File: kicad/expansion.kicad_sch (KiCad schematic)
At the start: 8 parts, among them J10 Slot 2, J11 Slot 3, J12 Slot 4, J9 Slot 1

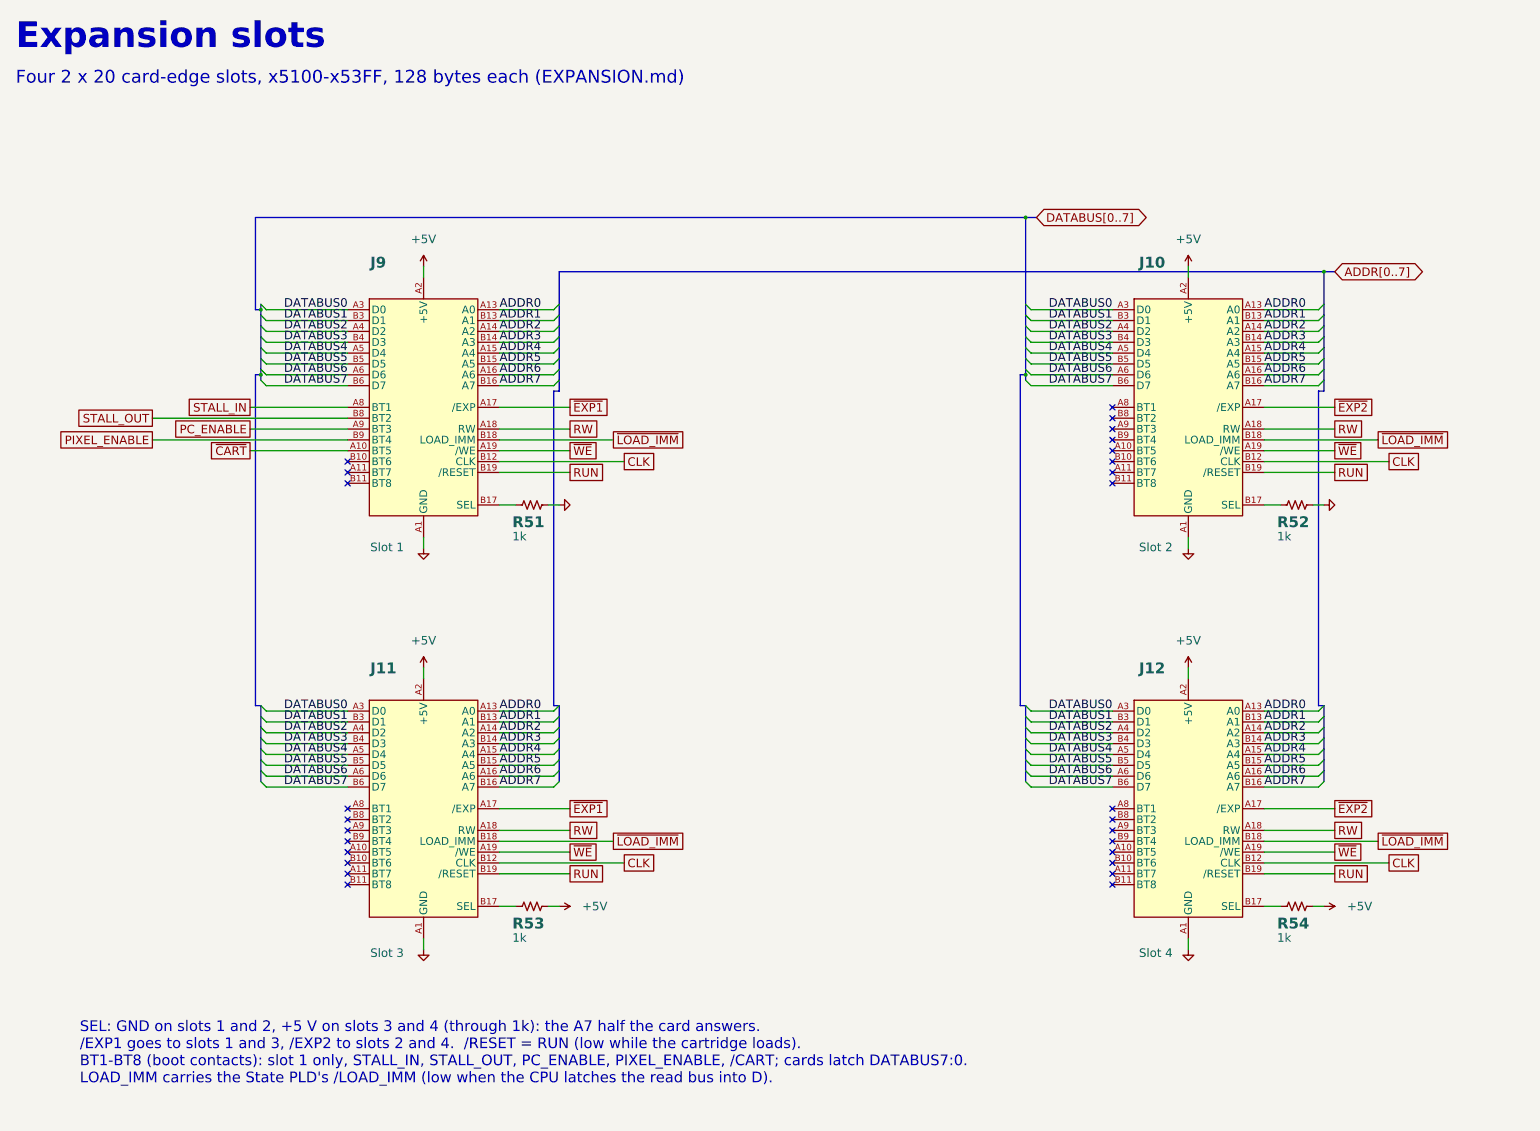
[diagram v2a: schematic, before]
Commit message: Expansion slots 2 x 25 (Sullins EBC25DRXH): A15:A8 and PIXEL_ENABLE on every slot
Contacts 1-20 unchanged; 21-24 = A8-A15, A25 = PIXEL_ENABLE, B25 = GND, so a
card can follow the video reads (HDMI capture) or CPU writes.  Footprint, 3D
model and shell keepout from Sullins drawing C10881 rev P (card 86.7 mm,
keepout 93.7 x 25.04 mm, 3.18 mm ear holes 78.11 apart, M3 x 12 + nut).
Schematic, netlist check, BOM (Digi-Key S3322-ND $6.63), EXPANSION.md
("Video capture cards"), CASE.md, BRINGUP.md, shell keepout drawing.
Main board file untouched: Justin updates the PCB from the schematic.

Co-Authored-By: Claude Opus 5.5 <noreply@anthropic.com>
Claude-Session: https://claude.ai/code/session_01DnW5SUDtmC2C2nXUS4xVk2
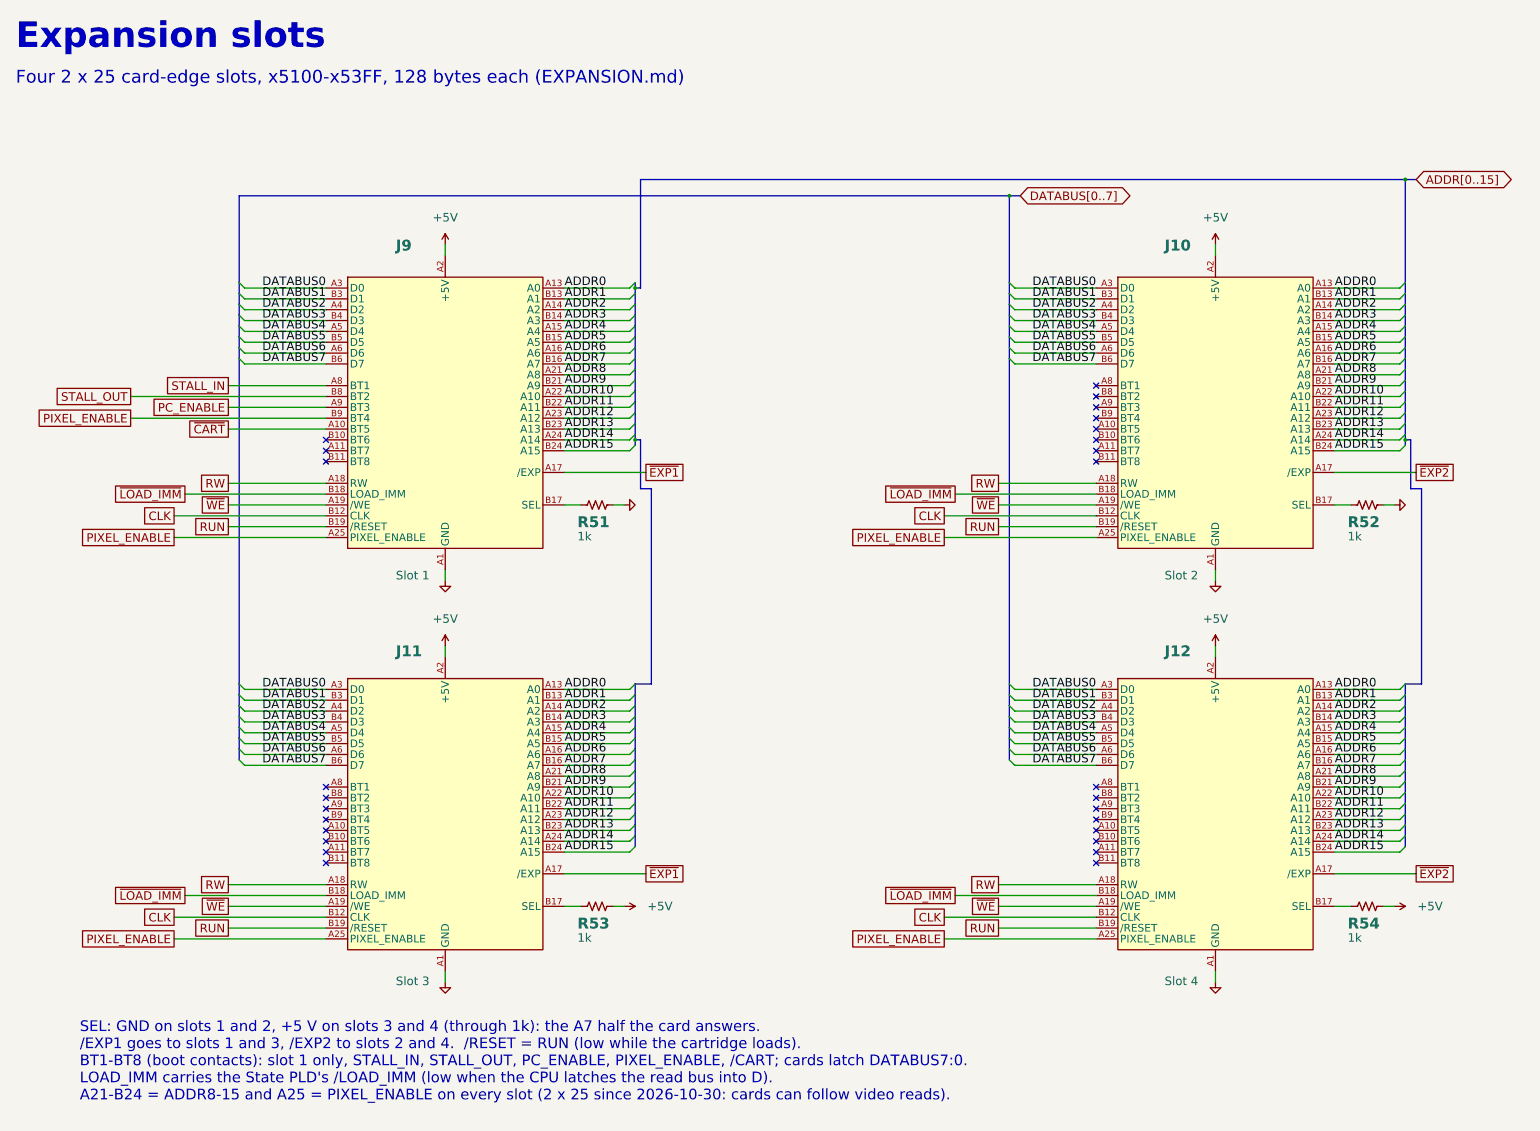
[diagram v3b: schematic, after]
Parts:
- J10, J11, J12, J9: footprint placard:CardEdge_2x20_P2.54mm_Vertical -> placard:CardEdge_2x25_P2.54mm_Vertical; MPN EBC20DCAN -> EBC25DRXH
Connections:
- net GND: now also J10.B25 (GND), J11.B25 (GND), J12.B25 (GND), J9.B25 (GND)
- net PIXEL_ENABLE: now also J10.A25 (PIXEL_ENABLE), J11.A25 (PIXEL_ENABLE), J12.A25 (PIXEL_ENABLE), J9.A25 (PIXEL_ENABLE)
- new net ADDR10: J10.A22 (A10), J11.A22 (A10), J12.A22 (A10), J9.A22 (A10)
- new net ADDR11: J10.B22 (A11), J11.B22 (A11), J12.B22 (A11), J9.B22 (A11)
- new net ADDR12: J10.A23 (A12), J11.A23 (A12), J12.A23 (A12), J9.A23 (A12)
- new net ADDR13: J10.B23 (A13), J11.B23 (A13), J12.B23 (A13), J9.B23 (A13)
- new net ADDR14: J10.A24 (A14), J11.A24 (A14), J12.A24 (A14), J9.A24 (A14)
- new net ADDR15: J10.B24 (A15), J11.B24 (A15), J12.B24 (A15), J9.B24 (A15)
- new net ADDR8: J10.A21 (A8), J11.A21 (A8), J12.A21 (A8), J9.A21 (A8)
- new net ADDR9: J10.B21 (A9), J11.B21 (A9), J12.B21 (A9), J9.B21 (A9)
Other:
- note added: "A21-B24 = ADDR8-15 and A25 = PIXEL_ENABLE on every slot (2 x 25 since 2026-10-30: cards can follow video reads)."
- note added: "Four 2 x 25 card-edge slots, x5100-x53FF, 128 bytes each (EXPANSION.md)"
- note removed: "Four 2 x 20 card-edge slots, x5100-x53FF, 128 bytes each (EXPANSION.md)"
- moved on the sheet: R51, R52, R53, R54

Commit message: Expansion slots use the cartridge's Molex 87715-9106
Justin, 2026-10-30: instead of the 2 x 25 EBC25DRXH (which would have moved
J9-J12 and U38/U42), the four expansion slots take the cartridge's 64-contact
connector.  Every slot has A15:A0, D7:D0, PIXEL_ENABLE, /HSYNC and /VSYNC.
The contacts a cartridge drives are left open, and every expansion output is
on a cartridge-slot spare, so neither does harm in the other's slot.
Footprint Molex_87715-9106_Expansion_Slot keeps the 72 mm card and its keepout
where the 2 x 20 slot had them (connector offset 7.63 mm), so nothing on the
board moves.  Schematic (netlist check 0 problems), symbol, 3D model,
EXPANSION.md pinout, CASE.md, BRINGUP.md, BOM ($199.47), keepout drawing.

Co-Authored-By: Claude Opus 5.5 <noreply@anthropic.com>
Claude-Session: https://claude.ai/code/session_01DnW5SUDtmC2C2nXUS4xVk2
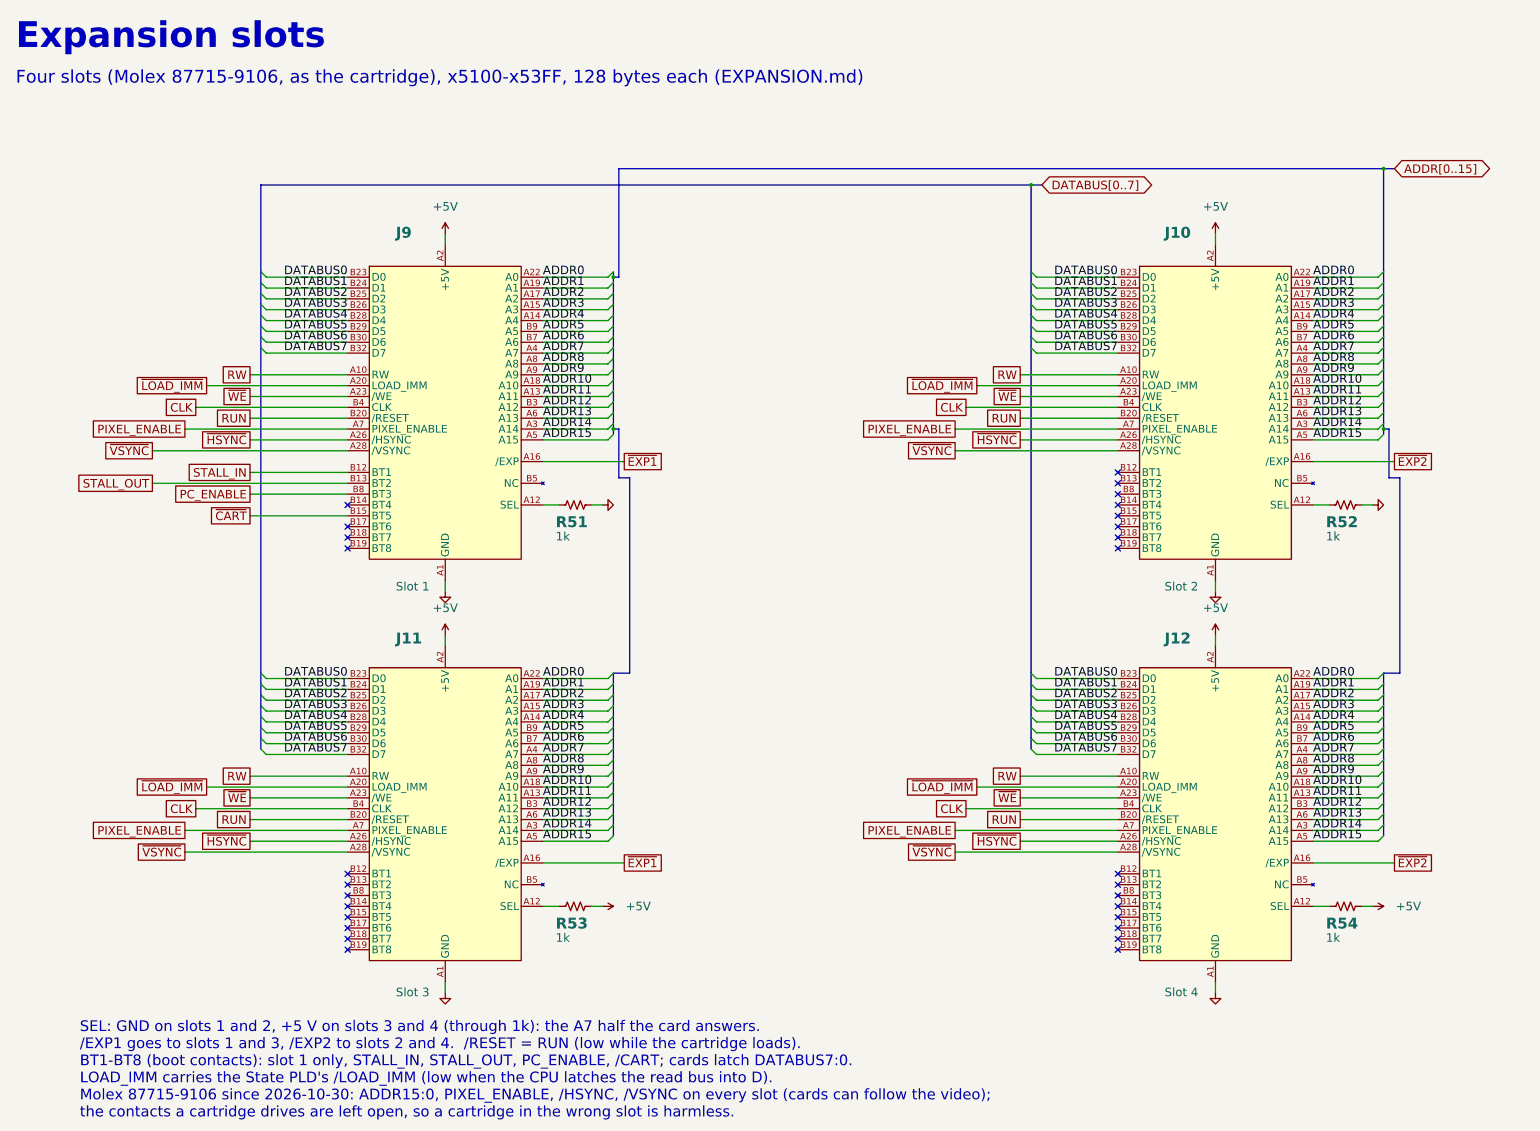
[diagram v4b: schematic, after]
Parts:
- J10, J11, J12, J9: footprint placard:CardEdge_2x25_P2.54mm_Vertical -> placard:Molex_87715-9106_Expansion_Slot; MPN EBC25DRXH -> 87715-9106; Manufacturer Sullins -> Molex
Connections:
- net ADDR0: now also J10.A22 (A0), J11.A22 (A0), J12.A22 (A0), J9.A22 (A0); no longer J10.A13 (A0), J11.A13 (A0), J12.A13 (A0), J9.A13 (A0)
- net ADDR1: now also J10.A19 (A1), J11.A19 (A1), J12.A19 (A1), J9.A19 (A1); no longer J10.B13 (A1), J11.B13 (A1), J12.B13 (A1), J9.B13 (A1)
- net ADDR10: now also J10.A18 (A10), J11.A18 (A10), J12.A18 (A10), J9.A18 (A10); no longer J10.A22 (A10), J11.A22 (A10), J12.A22 (A10), J9.A22 (A10)
- net ADDR11: now also J10.A13 (A11), J11.A13 (A11), J12.A13 (A11), J9.A13 (A11); no longer J10.B22 (A11), J11.B22 (A11), J12.B22 (A11), J9.B22 (A11)
- net ADDR12: now also J10.B3 (A12), J11.B3 (A12), J12.B3 (A12), J9.B3 (A12); no longer J10.A23 (A12), J11.A23 (A12), J12.A23 (A12), J9.A23 (A12)
- net ADDR13: now also J10.A6 (A13), J11.A6 (A13), J12.A6 (A13), J9.A6 (A13); no longer J10.B23 (A13), J11.B23 (A13), J12.B23 (A13), J9.B23 (A13)
- net ADDR14: now also J10.A3 (A14), J11.A3 (A14), J12.A3 (A14), J9.A3 (A14); no longer J10.A24 (A14), J11.A24 (A14), J12.A24 (A14), J9.A24 (A14)
- net ADDR15: now also J10.A5 (A15), J11.A5 (A15), J12.A5 (A15), J9.A5 (A15); no longer J10.B24 (A15), J11.B24 (A15), J12.B24 (A15), J9.B24 (A15)
- net ADDR2: now also J10.A17 (A2), J11.A17 (A2), J12.A17 (A2), J9.A17 (A2); no longer J10.A14 (A2), J11.A14 (A2), J12.A14 (A2), J9.A14 (A2)
- net ADDR3: now also J10.A15 (A3), J11.A15 (A3), J12.A15 (A3), J9.A15 (A3); no longer J10.B14 (A3), J11.B14 (A3), J12.B14 (A3), J9.B14 (A3)
- net ADDR4: now also J10.A14 (A4), J11.A14 (A4), J12.A14 (A4), J9.A14 (A4); no longer J10.A15 (A4), J11.A15 (A4), J12.A15 (A4), J9.A15 (A4)
- net ADDR5: now also J10.B9 (A5), J11.B9 (A5), J12.B9 (A5), J9.B9 (A5); no longer J10.B15 (A5), J11.B15 (A5), J12.B15 (A5), J9.B15 (A5)
- net ADDR6: now also J10.B7 (A6), J11.B7 (A6), J12.B7 (A6), J9.B7 (A6); no longer J10.A16 (A6), J11.A16 (A6), J12.A16 (A6), J9.A16 (A6)
- net ADDR7: now also J10.A4 (A7), J11.A4 (A7), J12.A4 (A7), J9.A4 (A7); no longer J10.B16 (A7), J11.B16 (A7), J12.B16 (A7), J9.B16 (A7)
- net ADDR8: now also J10.A8, J11.A8, J12.A8, J9.A8; no longer J10.A21 (A8), J11.A21 (A8), J12.A21 (A8), J9.A21 (A8)
- net ADDR9: now also J10.A9, J11.A9, J12.A9, J9.A9; no longer J10.B21 (A9), J11.B21 (A9), J12.B21 (A9), J9.B21 (A9)
- net CLK: now also J10.B4 (CLK), J11.B4 (CLK), J12.B4 (CLK), J9.B4 (CLK); no longer J10.B12 (CLK), J11.B12 (CLK), J12.B12 (CLK), J9.B12 (CLK)
- net DATABUS0: now also J10.B23 (D0), J11.B23 (D0), J12.B23 (D0), J9.B23 (D0); no longer J10.A3 (D0), J11.A3 (D0), J12.A3 (D0), J9.A3 (D0)
- net DATABUS1: now also J10.B24 (D1), J11.B24 (D1), J12.B24 (D1), J9.B24 (D1); no longer J10.B3 (D1), J11.B3 (D1), J12.B3 (D1), J9.B3 (D1)
- net DATABUS2: now also J10.B25 (D2), J11.B25 (D2), J12.B25 (D2), J9.B25 (D2); no longer J10.A4 (D2), J11.A4 (D2), J12.A4 (D2), J9.A4 (D2)
- net DATABUS3: now also J10.B26 (D3), J11.B26 (D3), J12.B26 (D3), J9.B26 (D3); no longer J10.B4 (D3), J11.B4 (D3), J12.B4 (D3), J9.B4 (D3)
- net DATABUS4: now also J10.B28 (D4), J11.B28 (D4), J12.B28 (D4), J9.B28 (D4); no longer J10.A5 (D4), J11.A5 (D4), J12.A5 (D4), J9.A5 (D4)
- net DATABUS5: now also J10.B29 (D5), J11.B29 (D5), J12.B29 (D5), J9.B29 (D5); no longer J10.B5 (D5), J11.B5 (D5), J12.B5 (D5), J9.B5 (D5)
- net DATABUS6: now also J10.B30 (D6), J11.B30 (D6), J12.B30 (D6), J9.B30 (D6); no longer J10.A6 (D6), J11.A6 (D6), J12.A6 (D6), J9.A6 (D6)
- net DATABUS7: now also J10.B32 (D7), J11.B32 (D7), J12.B32 (D7), J9.B32 (D7); no longer J10.B6 (D7), J11.B6 (D7), J12.B6 (D7), J9.B6 (D7)
- net GND: now also J10.A11 (GND), J10.A21 (GND), J10.A31 (GND), J10.B11 (GND), J10.B21 (GND), J10.B31 (GND), J11.A11 (GND), J11.A21 (GND), J11.A31 (GND), J11.B11 (GND), J11.B21 (GND), J11.B31 (GND), J12.A11 (GND), J12.A21 (GND), J12.A31 (GND), J12.B11 (GND), J12.B21 (GND), J12.B31 (GND), J9.A11 (GND), J9.A21 (GND), J9.A31 (GND), J9.B11 (GND), J9.B21 (GND), J9.B31 (GND); no longer J10.A12 (GND), J10.A20 (GND), J10.A7 (GND), J10.B20 (GND), J10.B25 (GND), J10.B7 (GND), J11.A12 (GND), J11.A20 (GND), J11.A7 (GND), J11.B20 (GND), J11.B25 (GND), J11.B7 (GND), J12.A12 (GND), J12.A20 (GND), J12.A7 (GND), J12.B20 (GND), J12.B25 (GND), J12.B7 (GND), J9.A12 (GND), J9.A20 (GND), J9.A7 (GND), J9.B20 (GND), J9.B25 (GND), J9.B7 (GND)
- net PC_ENABLE: now also J9.B8 (BT3); no longer J9.A9 (BT3)
- net PIXEL_ENABLE: now also J10.A7 (PIXEL_ENABLE), J11.A7 (PIXEL_ENABLE), J12.A7 (PIXEL_ENABLE), J9.A7 (PIXEL_ENABLE); no longer J10.A25 (PIXEL_ENABLE), J11.A25 (PIXEL_ENABLE), J12.A25 (PIXEL_ENABLE), J9.A25 (PIXEL_ENABLE), J9.B9 (BT4)
- net RUN: now also J10.B20 (/RESET), J11.B20 (/RESET), J12.B20 (/RESET), J9.B20 (/RESET); no longer J10.B19 (/RESET), J11.B19 (/RESET), J12.B19 (/RESET), J9.B19 (/RESET)
- net RW: now also J10.A10 (RW), J11.A10 (RW), J12.A10 (RW), J9.A10 (RW); no longer J10.A18 (RW), J11.A18 (RW), J12.A18 (RW), J9.A18 (RW)
- net STALL_IN: now also J9.B12 (BT1); no longer J9.A8 (BT1)
- net STALL_OUT: now also J9.B13 (BT2); no longer J9.B8 (BT2)
- net ~{CART}: now also J9.B15 (BT5); no longer J9.A10 (BT5)
- net ~{EXP1}: now also J11.A16 (/EXP), J9.A16 (/EXP); no longer J11.A17 (/EXP), J9.A17 (/EXP)
- net ~{EXP2}: now also J10.A16 (/EXP), J12.A16 (/EXP); no longer J10.A17 (/EXP), J12.A17 (/EXP)
- net ~{LOAD_IMM}: now also J10.A20 (LOAD_IMM), J11.A20 (LOAD_IMM), J12.A20 (LOAD_IMM), J9.A20 (LOAD_IMM); no longer J10.B18 (LOAD_IMM), J11.B18 (LOAD_IMM), J12.B18 (LOAD_IMM), J9.B18 (LOAD_IMM)
- net ~{WE}: now also J10.A23 (/WE), J11.A23 (/WE), J12.A23 (/WE), J9.A23 (/WE); no longer J10.A19 (/WE), J11.A19 (/WE), J12.A19 (/WE), J9.A19 (/WE)
- net at J11.B10 (NC): now also J11.A24 (NC), J11.A25 (NC), J11.A27 (NC), J11.A29 (NC), J11.A30 (NC), J11.A32 (NC), J11.B16 (NC), J11.B22 (NC), J11.B27 (NC), J11.B5 (NC), J11.B6 (NC)
- net at R53.1: now also J11.A12 (SEL); no longer J11.B17 (SEL)
- net at J12.B10 (NC): now also J12.A24 (NC), J12.A25 (NC), J12.A27 (NC), J12.A29 (NC), J12.A30 (NC), J12.A32 (NC), J12.B16 (NC), J12.B22 (NC), J12.B27 (NC), J12.B5 (NC), J12.B6 (NC)
- net at R54.1: now also J12.A12 (SEL); no longer J12.B17 (SEL)
- net at R51.1: now also J9.A12 (SEL); no longer J9.B17 (SEL)
- net at J10.B10 (NC): now also J10.A24 (NC), J10.A25 (NC), J10.A27 (NC), J10.A29 (NC), J10.A30 (NC), J10.A32 (NC), J10.B16 (NC), J10.B22 (NC), J10.B27 (NC), J10.B5 (NC), J10.B6 (NC)
- net at R52.1: now also J10.A12 (SEL); no longer J10.B17 (SEL)
- net at J9.B10 (NC): now also J9.A24 (NC), J9.A25 (NC), J9.A27 (NC), J9.A29 (NC), J9.A30 (NC), J9.A32 (NC), J9.B16 (NC), J9.B22 (NC), J9.B27 (NC), J9.B5 (NC), J9.B6 (NC)
- new net ~{HSYNC}: J10.A26 (/HSYNC), J11.A26 (/HSYNC), J12.A26 (/HSYNC), J9.A26 (/HSYNC)
- new net ~{VSYNC}: J10.A28 (/VSYNC), J11.A28 (/VSYNC), J12.A28 (/VSYNC), J9.A28 (/VSYNC)
- no-connect marks 27 -> 28
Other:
- note added: "BT1-BT8 (boot contacts): slot 1 only, STALL_IN, STALL_OUT, PC_ENABLE, /CART; cards latch DATABUS7:0."
- note added: "Four slots (Molex 87715-9106, as the cartridge), x5100-x53FF, 128 bytes each (EXPANSION.md)"
- note added: "Molex 87715-9106 since 2026-10-30: ADDR15:0, PIXEL_ENABLE, /HSYNC, /VSYNC on every slot (cards can follow the video);"
- note added: "the contacts a cartridge drives are left open, so a cartridge in the wrong slot is harmless."
- note removed: "A21-B24 = ADDR8-15 and A25 = PIXEL_ENABLE on every slot (2 x 25 since 2026-10-30: cards can follow video reads)."
- note removed: "BT1-BT8 (boot contacts): slot 1 only, STALL_IN, STALL_OUT, PC_ENABLE, PIXEL_ENABLE, /CART; cards latch DATABUS7:0."
- note removed: "Four 2 x 25 card-edge slots, x5100-x53FF, 128 bytes each (EXPANSION.md)"
- moved on the sheet: R51, R52, R53, R54
